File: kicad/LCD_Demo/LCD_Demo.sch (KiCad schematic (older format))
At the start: 11 parts, among them IC1 PIC16LF19156-I_SP, J1 ICSP

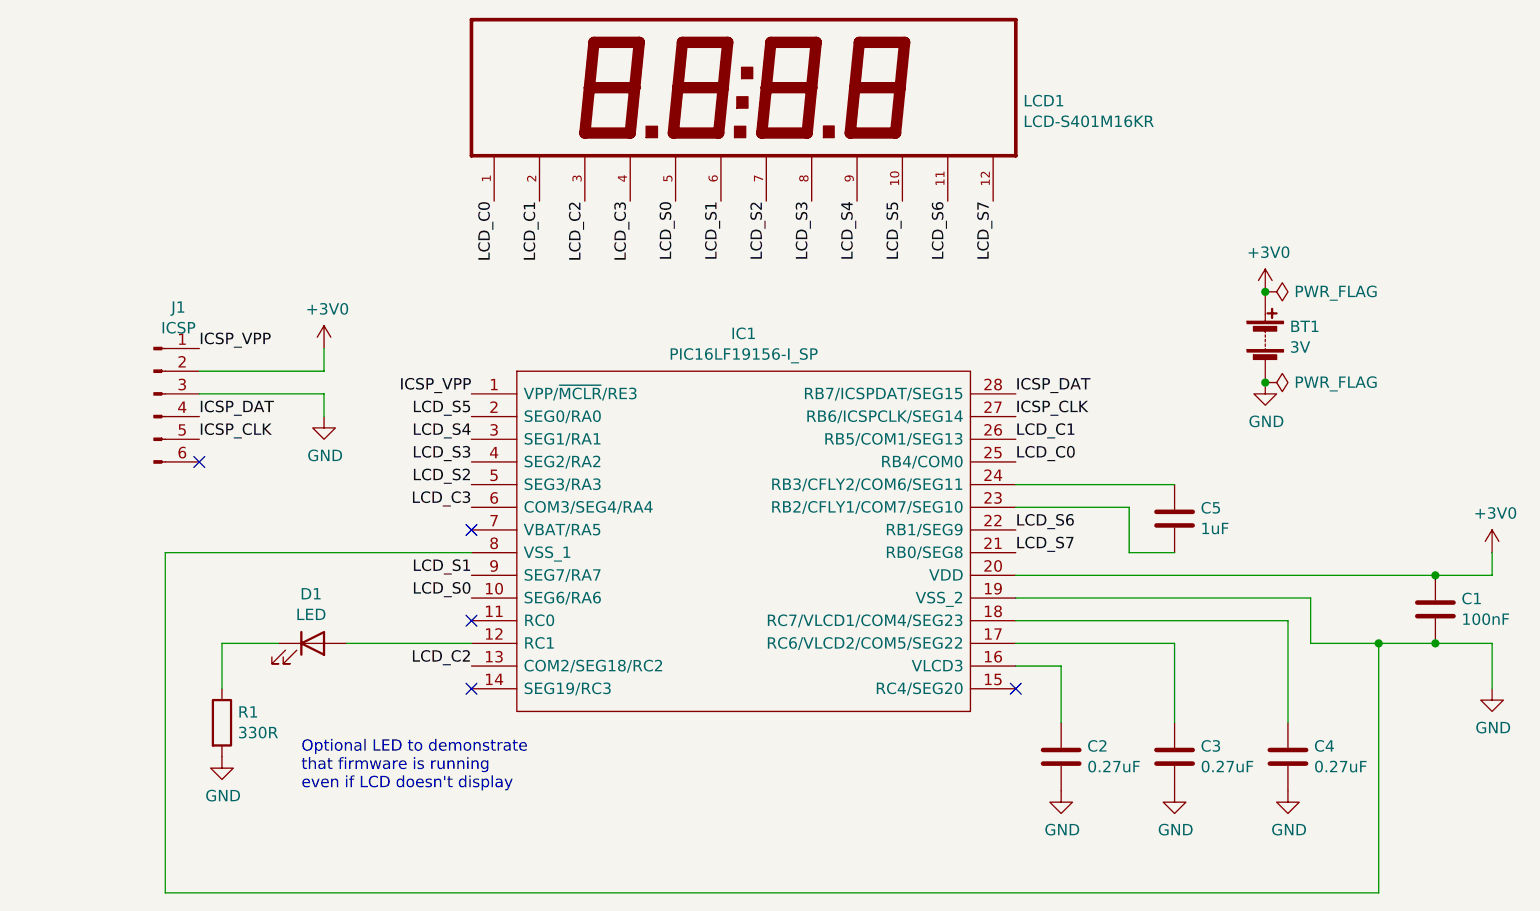
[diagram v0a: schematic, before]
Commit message: README changes, make LCD work, add PIC12F1572 test generator
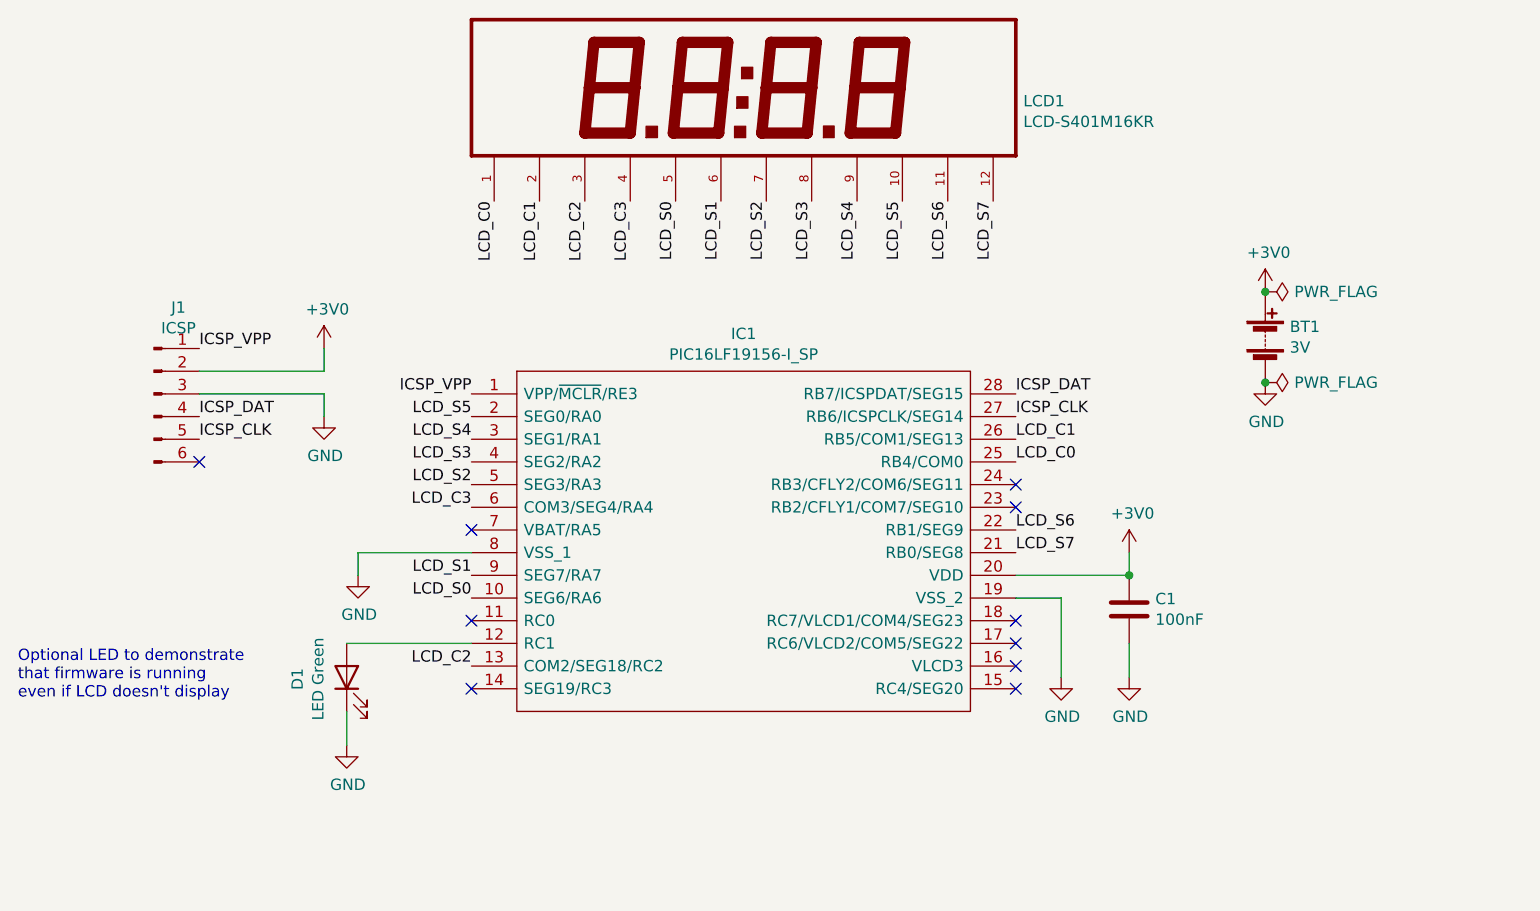
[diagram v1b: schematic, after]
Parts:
- removed C2, C3, C4: 0.27uF, Capacitor_THT:C_Disc_D3.0mm_W1.6mm_P2.50mm, symbol Device:C
- removed C5: 1uF, Capacitor_THT:C_Disc_D3.0mm_W1.6mm_P2.50mm, symbol Device:C
- removed R1: 330R, Resistor_THT:R_Axial_DIN0207_L6.3mm_D2.5mm_P7.62mm_Horizontal, symbol Device:R
- D1: value LED -> LED Green
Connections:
- net GND: now also D1.1 (K)
- no-connect marks 5 -> 10
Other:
- moved on the sheet: C1, D1
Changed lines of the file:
@@
 Rev "REV0"
 Comp "Karen A Morrissey"
-Comment1 "A minimal circuit for driving a 1/4 multiplexed segment LCD with charge pump"
+Comment1 "Minimal circuit for driving a multiplexed LCD glass from a PIC with an LCD driver module"
 Comment2 ""
 Comment3 ""
@@
 L Device:C C1
 U 1 1 6087F77C
-P 8250 4650
-F 0 "C1" H 8365 4696 50  0000 L CNN
-F 1 "100nF" H 8365 4605 50  0000 L CNN
-F 2 "Capacitor_THT:C_Disc_D3.0mm_W1.6mm_P2.50mm" H 8288 4500 50  0001 C CNN
-F 3 "~" H 8250 4650 50  0001 C CNN
-	1    8250 4650
+P 6900 4650
+F 0 "C1" H 7015 4696 50  0000 L CNN
+F 1 "100nF" H 7015 4605 50  0000 L CNN
+F 2 "Capacitor_THT:C_Disc_D3.0mm_W1.6mm_P2.50mm" H 6938 4500 50  0001 C CNN
+F 3 "~" H 6900 4650 50  0001 C CNN
+	1    6900 4650
 	1    0    0    -1
 $EndComp
@@
 L Device:LED D1
 U 1 1 6087FCFA
-P 3300 4800
-F 0 "D1" H 3293 5017 50  0000 C CNN
-F 1 "LED" H 3293 4926 50  0000 C CNN
-F 2 "LED_THT:LED_D5.0mm" H 3300 4800 50  0001 C CNN
-F 3 "~" H 3300 4800 50  0001 C CNN
-	1    3300 4800
-	1    0    0    -1
-$EndComp
-$Comp
-L Device:R R1
-U 1 1 608808E6
-P 2900 5150
-F 0 "R1" H 2970 5196 50  0000 L CNN
-F 1 "330R" H 2970 5105 50  0000 L CNN
-F 2 "Resistor_THT:R_Axial_DIN0207_L6.3mm_D2.5mm_P7.62mm_Horizontal" V 2830 5150 50  0001 C CNN
-F 3 "~" H 2900 5150 50  0001 C CNN
-	1    2900 5150
-	1    0    0    -1
+P 3450 4950
+F 0 "D1" H 3443 5167 50  0000 C CNN
+F 1 "LED Green" H 3443 5076 50  0000 C CNN
+F 2 "LED_THT:LED_D5.0mm" H 3450 4950 50  0001 C CNN
+F 3 "~" H 3450 4950 50  0001 C CNN
+	1    3450 4950
+	0    -1   -1   0
 $EndComp
 $Comp
 L power:GND #PWR0101
 U 1 1 60882FBD
-P 2900 5300
-F 0 "#PWR0101" H 2900 5050 50  0001 C CNN
-F 1 "GND" H 2905 5127 50  0000 C CNN
-F 2 "" H 2900 5300 50  0001 C CNN
-F 3 "" H 2900 5300 50  0001 C CNN
-	1    2900 5300
+P 3450 5250
+F 0 "#PWR0101" H 3450 5000 50  0001 C CNN
+F 1 "GND" H 3455 5077 50  0000 C CNN
+F 2 "" H 3450 5250 50  0001 C CNN
+F 3 "" H 3450 5250 50  0001 C CNN
+	1    3450 5250
 	1    0    0    -1
 $EndComp
@@
 Wire Wire Line
 	4000 4800 3450 4800
-Wire Wire Line
-	3150 4800 2900 4800
 Text Label 4100 2850 3    50   ~ 0
 LCD_C0
@@
 L power:+3V0 #PWR0104
 U 1 1 608895FE
-P 8500 4400
-F 0 "#PWR0104" H 8500 4250 50  0001 C CNN
-F 1 "+3V0" H 8515 4573 50  0000 C CNN
-F 2 "" H 8500 4400 50  0001 C CNN
-F 3 "" H 8500 4400 50  0001 C CNN
-	1    8500 4400
+P 6900 4400
+F 0 "#PWR0104" H 6900 4250 50  0001 C CNN
+F 1 "+3V0" H 6915 4573 50  0000 C CNN
+F 2 "" H 6900 4400 50  0001 C CNN
+F 3 "" H 6900 4400 50  0001 C CNN
+	1    6900 4400
 	1    0    0    -1
 $EndComp
@@
 L power:GND #PWR0105
 U 1 1 6088985E
-P 8500 5000
-F 0 "#PWR0105" H 8500 4750 50  0001 C CNN
-F 1 "GND" H 8505 4827 50  0000 C CNN
-F 2 "" H 8500 5000 50  0001 C CNN
-F 3 "" H 8500 5000 50  0001 C CNN
-	1    8500 5000
+P 6900 4950
+F 0 "#PWR0105" H 6900 4700 50  0001 C CNN
+F 1 "GND" H 6905 4777 50  0000 C CNN
+F 2 "" H 6900 4950 50  0001 C CNN
+F 3 "" H 6900 4950 50  0001 C CNN
+	1    6900 4950
 	1    0    0    -1
 $EndComp
@@
 LCD_S0
 Wire Wire Line
-	8250 4500 8500 4500
-Wire Wire Line
-	8500 4500 8500 4400
-Wire Wire Line
-	8250 4800 8500 4800
-Wire Wire Line
-	8500 4800 8500 5000
-Wire Wire Line
-	2650 4400 4000 4400
-Wire Wire Line
 	3350 3600 3350 3500
 Wire Wire Line
 	3350 3700 3350 3800
-$Comp
-L Device:C C2
-U 1 1 608649D5
-P 6600 5300
-F 0 "C2" H 6715 5346 50  0000 L CNN
-F 1 "0.27uF" H 6715 5255 50  0000 L CNN
-F 2 "Capacitor_THT:C_Disc_D3.0mm_W1.6mm_P2.50mm" H 6638 5150 50  0001 C CNN
-F 3 "~" H 6600 5300 50  0001 C CNN
-	1    6600 5300
-	1    0    0    -1
-$EndComp
-$Comp
-L Device:C C3
-U 1 1 60865017
-P 7100 5300
-F 0 "C3" H 7215 5346 50  0000 L CNN
-F 1 "0.27uF" H 7215 5255 50  0000 L CNN
-F 2 "Capacitor_THT:C_Disc_D3.0mm_W1.6mm_P2.50mm" H 7138 5150 50  0001 C CNN
-F 3 "~" H 7100 5300 50  0001 C CNN
-	1    7100 5300
-	1    0    0    -1
-$EndComp
-$Comp
-L Device:C C4
-U 1 1 608652E1
-P 7600 5300
-F 0 "C4" H 7715 5346 50  0000 L CNN
-F 1 "0.27uF" H 7715 5255 50  0000 L CNN
-F 2 "Capacitor_THT:C_Disc_D3.0mm_W1.6mm_P2.50mm" H 7638 5150 50  0001 C CNN
-F 3 "~" H 7600 5300 50  0001 C CNN
-	1    7600 5300
-	1    0    0    -1
-$EndComp
-$Comp
-L Device:C C5
-U 1 1 608655BD
-P 7100 4250
-F 0 "C5" H 7215 4296 50  0000 L CNN
-F 1 "1uF" H 7215 4205 50  0000 L CNN
-F 2 "Capacitor_THT:C_Disc_D3.0mm_W1.6mm_P2.50mm" H 7138 4100 50  0001 C CNN
-F 3 "~" H 7100 4250 50  0001 C CNN
-	1    7100 4250
-	1    0    0    -1
-$EndComp
-Wire Wire Line
-	6400 4100 7100 4100
-Wire Wire Line
-	6400 4200 6900 4200
-Wire Wire Line
-	6900 4200 6900 4400
-Wire Wire Line
-	6900 4400 7100 4400
-Wire Wire Line
-	6400 4900 6600 4900
-Wire Wire Line
-	6600 4900 6600 5150
-Wire Wire Line
-	6400 4800 7100 4800
-Wire Wire Line
-	7100 4800 7100 5150
-Wire Wire Line
-	6400 4700 7600 4700
-Wire Wire Line
-	7600 4700 7600 5150
-Wire Wire Line
-	7700 4600 7700 4800
-Wire Wire Line
-	7700 4800 8000 4800
-Wire Wire Line
-	6400 4600 7700 4600
 $Comp
 L power:GND #PWR03
 U 1 1 60867753
-P 6600 5450
-F 0 "#PWR03" H 6600 5200 50  0001 C CNN
-F 1 "GND" H 6605 5277 50  0000 C CNN
-F 2 "" H 6600 5450 50  0001 C CNN
-F 3 "" H 6600 5450 50  0001 C CNN
-	1    6600 5450
-	1    0    0    -1
-$EndComp
-$Comp
-L power:GND #PWR04
-U 1 1 60867A4B
-P 7100 5450
-F 0 "#PWR04" H 7100 5200 50  0001 C CNN
-F 1 "GND" H 7105 5277 50  0000 C CNN
-F 2 "" H 7100 5450 50  0001 C CNN
-F 3 "" H 7100 5450 50  0001 C CNN
-	1    7100 5450
-	1    0    0    -1
-$EndComp
-$Comp
-L power:GND #PWR05
-U 1 1 60867D4F
-P 7600 5450
-F 0 "#PWR05" H 7600 5200 50  0001 C CNN
-F 1 "GND" H 7605 5277 50  0000 C CNN
-F 2 "" H 7600 5450 50  0001 C CNN
-F 3 "" H 7600 5450 50  0001 C CNN
-	1    7600 5450
-	1    0    0    -1
-$EndComp
-Wire Wire Line
-	2650 5900 8000 5900
-Wire Wire Line
-	8000 5900 8000 4800
-Wire Wire Line
-	2650 4400 2650 5900
-Connection ~ 8000 4800
-Wire Wire Line
-	6400 4500 8250 4500
-Connection ~ 8250 4500
-Wire Wire Line
-	8000 4800 8250 4800
-Connection ~ 8250 4800
-Text Notes 3250 5450 0    50   ~ 0
+P 3500 4500
+F 0 "#PWR03" H 3500 4250 50  0001 C CNN
+F 1 "GND" H 3505 4327 50  0000 C CNN
+F 2 "" H 3500 4500 50  0001 C CNN
+F 3 "" H 3500 4500 50  0001 C CNN
+	1    3500 4500
+	1    0    0    -1
+$EndComp
+Text Notes 2000 5050 0    50   ~ 0
 Optional LED to demonstrate\nthat firmware is running\neven if LCD doesn't display
 Wire Wire Line
-	2900 4800 2900 5000
+	4000 4400 3500 4400
+NoConn ~ 6400 4900
+NoConn ~ 6400 4800
+NoConn ~ 6400 4700
+NoConn ~ 6400 4200
+NoConn ~ 6400 4100
+Wire Wire Line
+	6400 4500 6900 4500
+Wire Wire Line
+	6600 4600 6400 4600
+Wire Wire Line
+	3450 5100 3450 5250
+$Comp
+L power:GND #PWR?
+U 1 1 60AF36F4
+P 6600 4950
+F 0 "#PWR?" H 6600 4700 50  0001 C CNN
+F 1 "GND" H 6605 4777 50  0000 C CNN
+F 2 "" H 6600 4950 50  0001 C CNN
+F 3 "" H 6600 4950 50  0001 C CNN
+	1    6600 4950
+	1    0    0    -1
+$EndComp
+Wire Wire Line
+	6900 4500 6900 4400
+Connection ~ 6900 4500
+Wire Wire Line
+	6900 4800 6900 4950
+Wire Wire Line
+	6600 4600 6600 4950
+Wire Wire Line
+	3500 4400 3500 4500
 $EndSCHEMATC
